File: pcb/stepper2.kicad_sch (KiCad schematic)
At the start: 61 parts, among them J1 DA15_Receptacle_MountingHoles, J10 Conn_01x07_Pin, J11 FAN, J12 Conn_01x03_Pin, J13 Conn_01x03_Pin, J14 Conn_01x03_Pin, J2 DA15_Receptacle_MountingHoles, J3 DA15_Receptacle_MountingHoles, J4 DE15_Receptacle_HighDensity, J5 DE15_Receptacle_HighDensity, J6 DE15_Receptacle_HighDensity, J7 Conn_01x04_Pin, J8 Conn_01x05_Pin, J9 Conn_01x06_Pin, SW1 SW_Push, U1 AM26LS32ACN, U2 AM26LS32Ax, U3 AM26LS32ACN, U4 TMC2209_BIGTREETECH, U5 TMC2209_BIGTREETECH, U6 TMC2209_BIGTREETECH

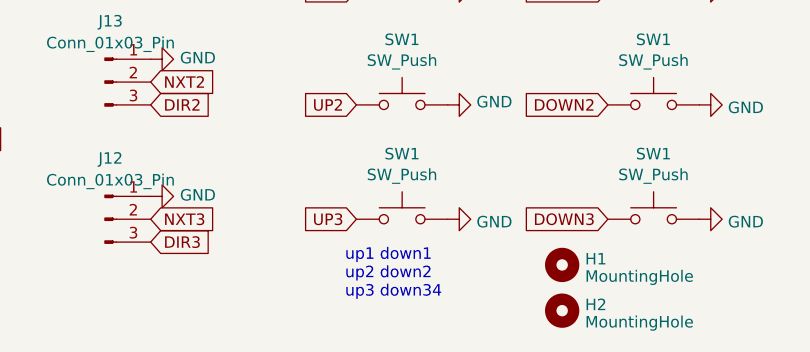
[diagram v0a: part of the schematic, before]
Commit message: fixed typo in schematics
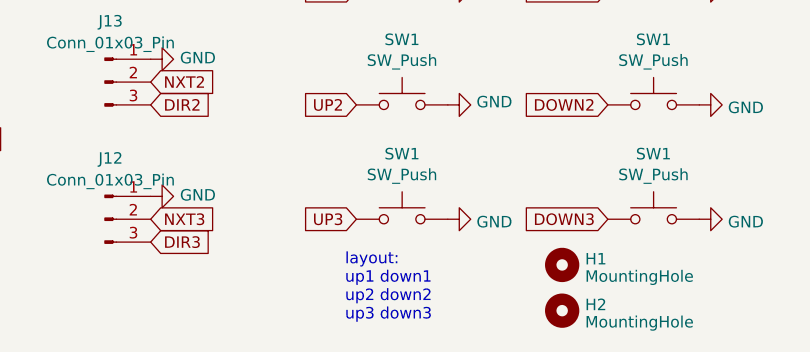
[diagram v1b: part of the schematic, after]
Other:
- note added: "layout: up1 down1 up2 down2 up3 down3"
- note removed: "up1 down1 up2 down2 up3 down34"
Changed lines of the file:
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@@
     (stroke (width 0) (type default))
   )
-  (text "up1 down1\nup2 down2\nup3 down34\n" (at 125.73 194.31 0)
+  (text "layout:\nup1 down1\nup2 down2\nup3 down3\n" (at 125.73 196.85 0)
     (effects (font (size 1.27 1.27)) (justify left bottom))
   )

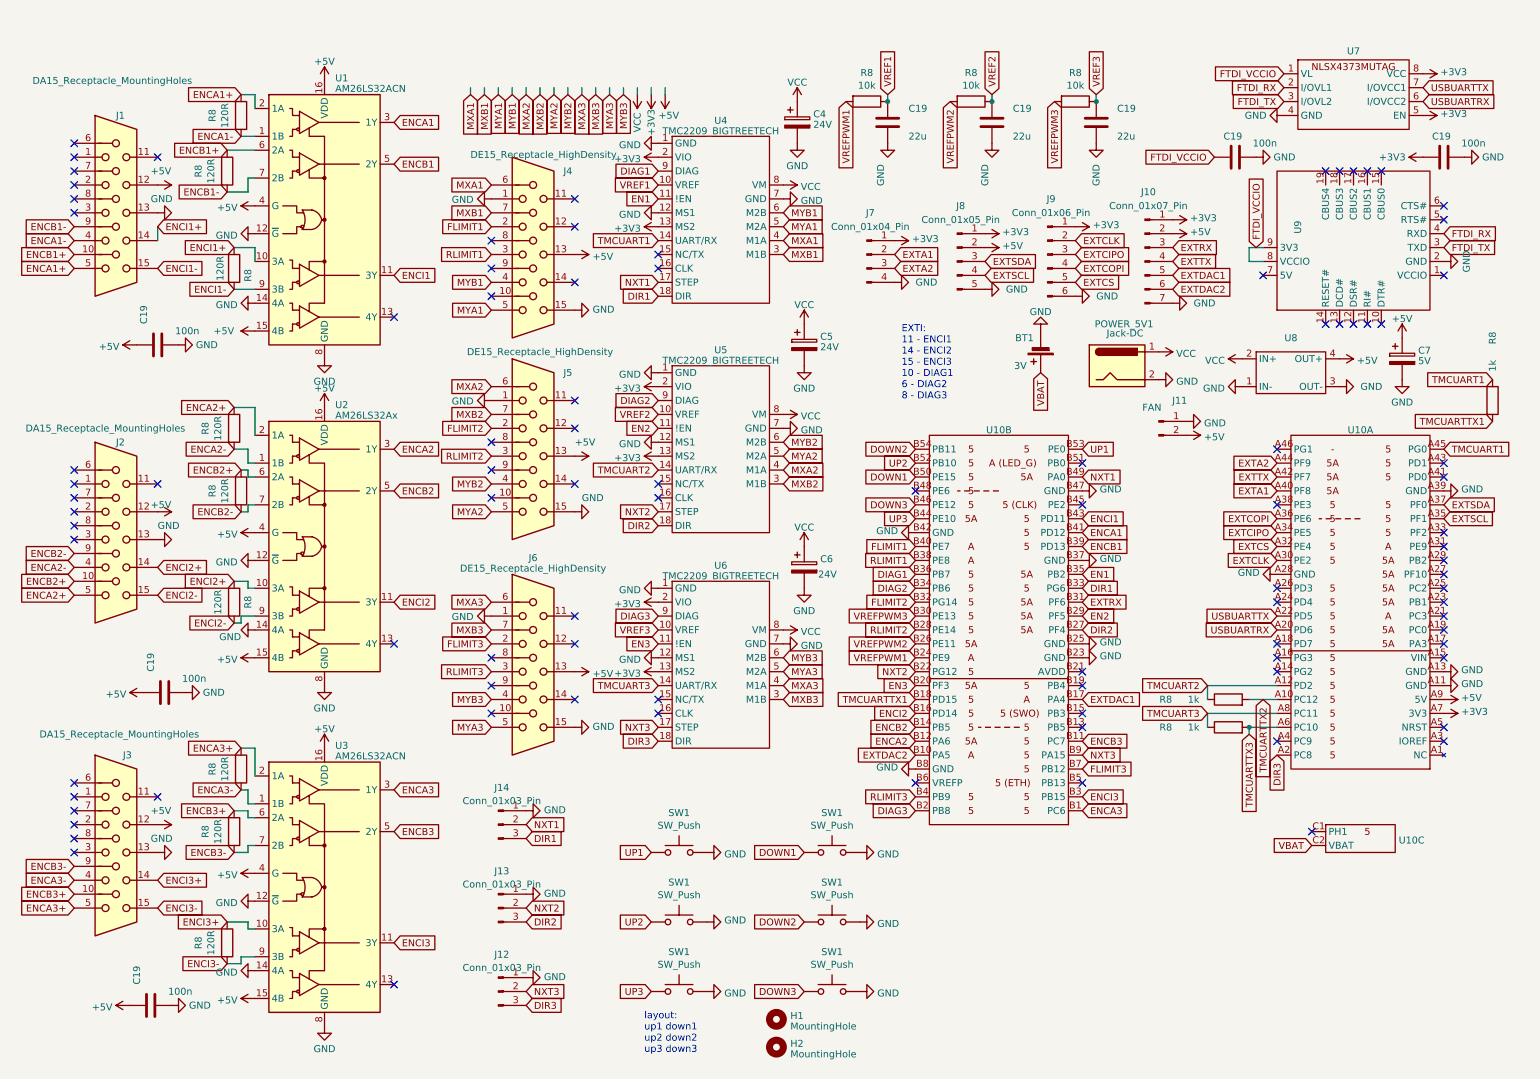
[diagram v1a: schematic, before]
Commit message: PCB updated to use active and available components; added mpn numbers
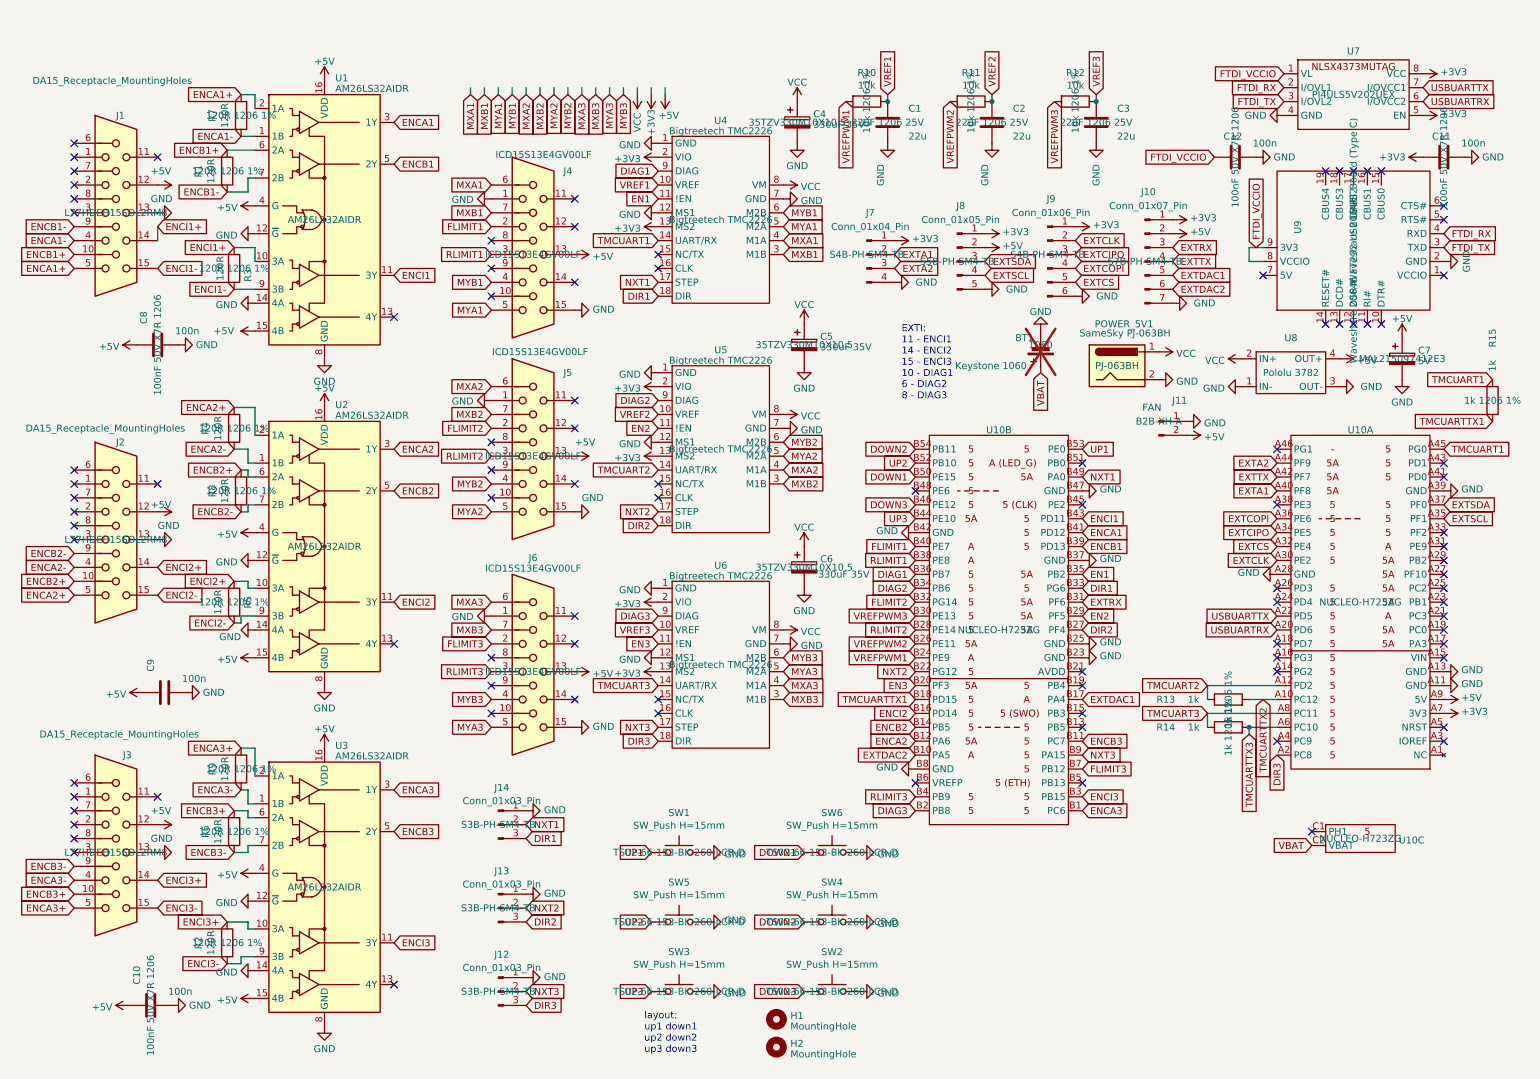
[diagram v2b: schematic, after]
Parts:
- BT1: value 3V -> Keystone 1060; mpn (none) -> 1060; now not fitted
- C1, C2, C3: renamed from C19; mpn (none) -> 22uF 1206 25V
- C10, C11, C12, C8, C9: renamed from C19; mpn (none) -> 100nF 50V X7R 1206
- C4, C5, C6: value 24V -> 330uF 35V; mpn (none) -> 35TZV330M10X10.5
- C7: mpn (none) -> MAL215097412E3
- J1, J2, J3: mpn (none) -> L77HDEH15SOL2RM8
- J10: mpn (none) -> S7B-PH-SM4-TB
- J11: mpn (none) -> B2B-XH-A
- J12, J13, J14: mpn (none) -> S3B-PH-SM4-TB
- J4, J5, J6: value DE15_Receptacle_HighDensity -> ICD15S13E4GV00LF; mpn (none) -> ICD15S13E4GV00LF
- J7, J9: mpn (none) -> S4B-PH-SM4-TB
- J8: mpn (none) -> S5B-PH-SM4-TB
- POWER_5V1: value Jack-DC -> SameSky PJ-063BH; mpn (none) -> PJ-063BH
- R1, R2, R3, R4, R5, R6, R7, R9: renamed from R8; mpn (none) -> 120R 1206 1%
- R10, R11, R12: renamed from R8; mpn (none) -> 10k 1206 1%
- R13, R14, R15: renamed from R8; mpn (none) -> 1k 1206 1%
- R8: mpn (none) -> 120R 1206 1%
- SW1: value SW_Push -> SW_Push H=15mm; footprint Button_Switch_SMD:SW_Push_1P1T_NO_6x6mm_H9.5mm -> Button_Switch_THT:SW_PUSH_6mm_H4.3mm; LCSC C620327 -> (none); mpn (none) -> TS02-66-153-BK-260-LCR-D
- SW2, SW3, SW4, SW5, SW6: renamed from SW1; value SW_Push -> SW_Push H=15mm; footprint Button_Switch_SMD:SW_Push_1P1T_NO_6x6mm_H9.5mm -> Button_Switch_THT:SW_PUSH_6mm_H4.3mm; LCSC C620327 -> (none); mpn (none) -> TS02-66-153-BK-260-LCR-D
- U1, U3: value AM26LS32ACN -> AM26LS32AIDR; mpn (none) -> AM26LS32AIDR
- U10: mpn (none) -> NUCLEO-H723ZG
- U2: value AM26LS32Ax -> AM26LS32AIDR; mpn (none) -> AM26LS32AIDR
- U4, U5, U6: value TMC2209_BIGTREETECH -> Bigtreetech TMC2226; mpn (none) -> Bigtreetech TMC2226
- U7: footprint stepper2:UDFN-8_1.2x1.8mm_OR_SO8_3.9x4.9mm -> Package_SO:MSOP-8_3x3mm_P0.65mm; LCSC C604194 -> C481697; mpn (none) -> PI4ULS5V202UEX
- U8: footprint stepper2:DCDC_17.0mm_22.2mm -> stepper2:POLOLU_3782; mpn (none) -> Pololu 3782
- U9: value ~ -> Waveshare 20646 FT232 USB UART Board (Type C); mpn (none) -> Waveshare 20646

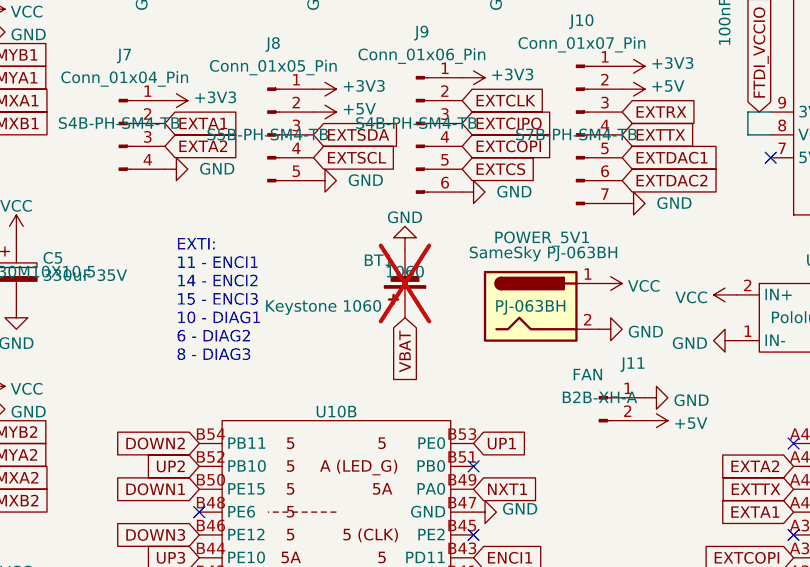
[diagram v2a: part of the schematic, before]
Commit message: reverted DNP flag for 3V battery
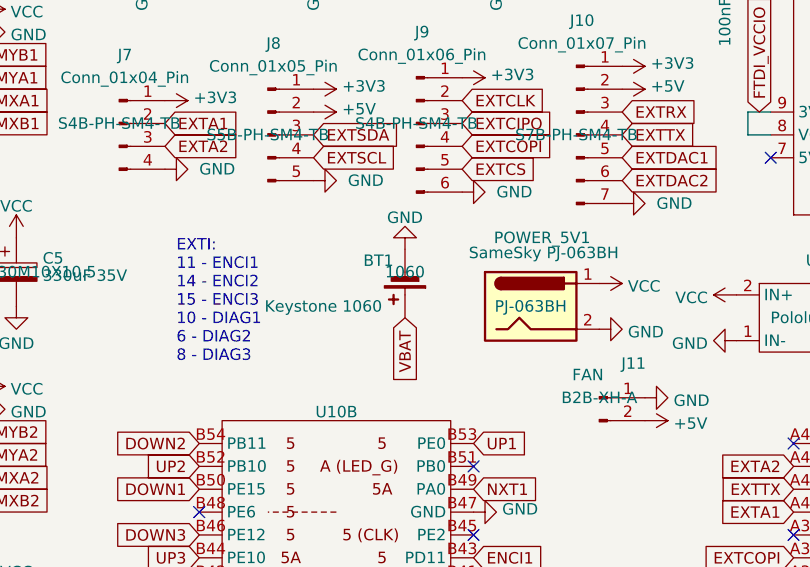
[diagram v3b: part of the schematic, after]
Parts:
- BT1: now fitted
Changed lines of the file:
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@@
 		(in_bom yes)
 		(on_board yes)
-		(dnp yes)
+		(dnp no)
 		(property "Reference" "BT1"
 			(at 196.85 66.04 0)

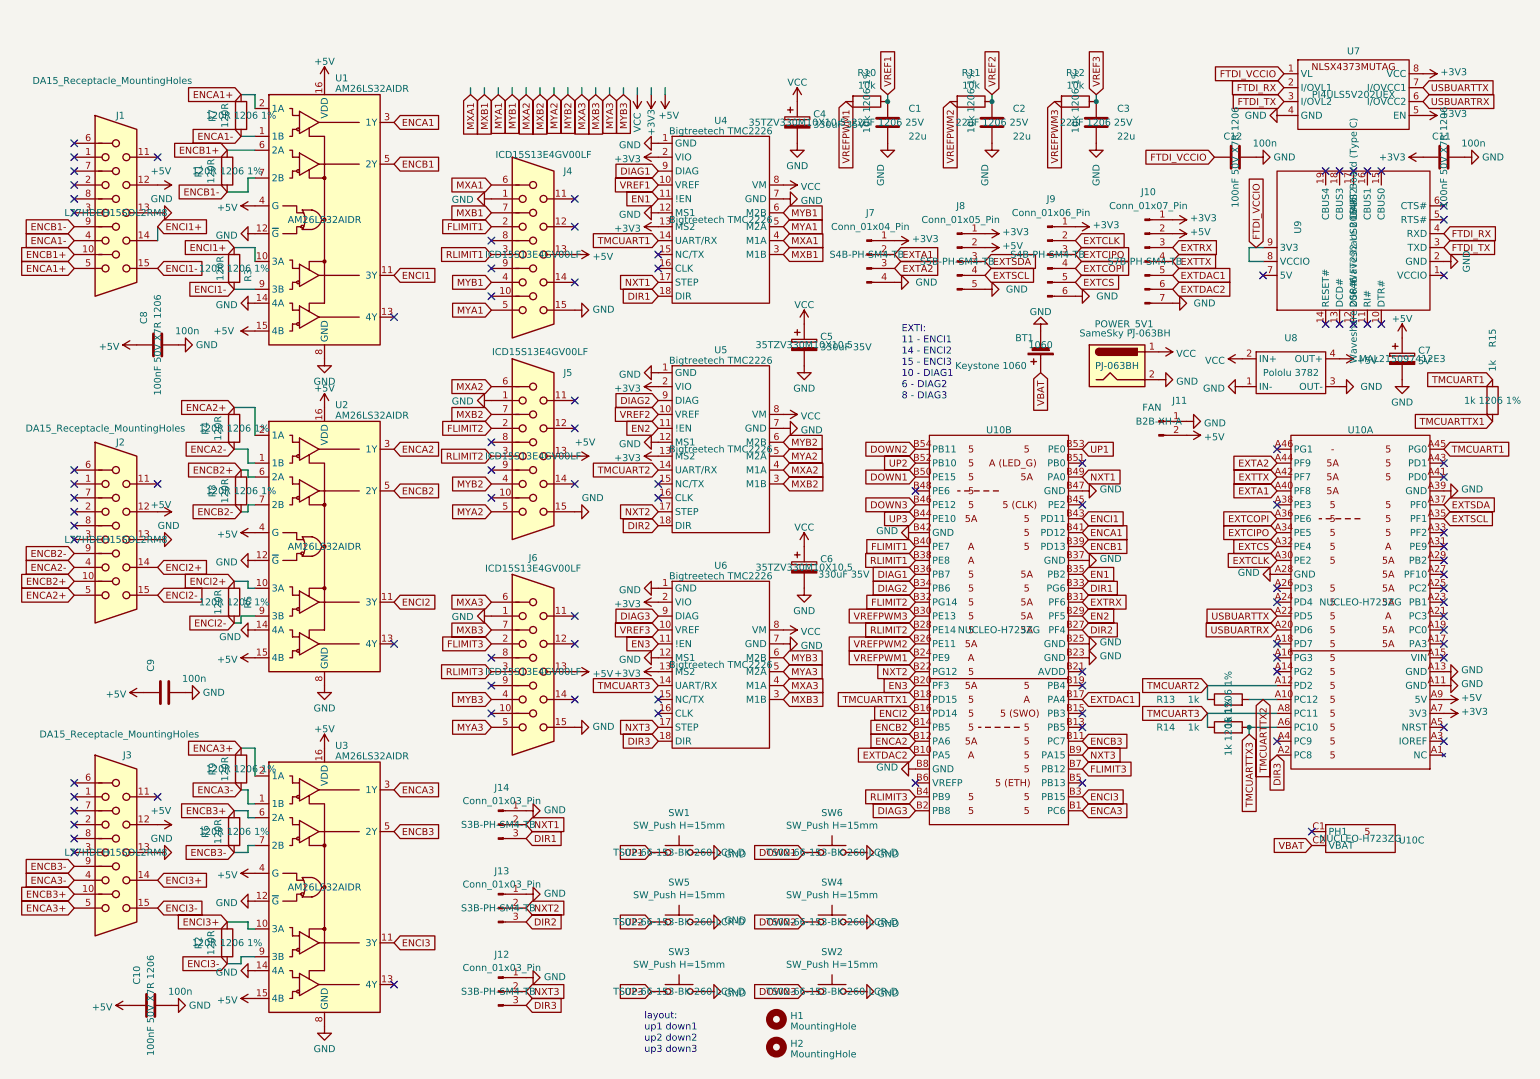
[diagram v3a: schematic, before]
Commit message: non-standard components marked as DNP for easier assembly ordering
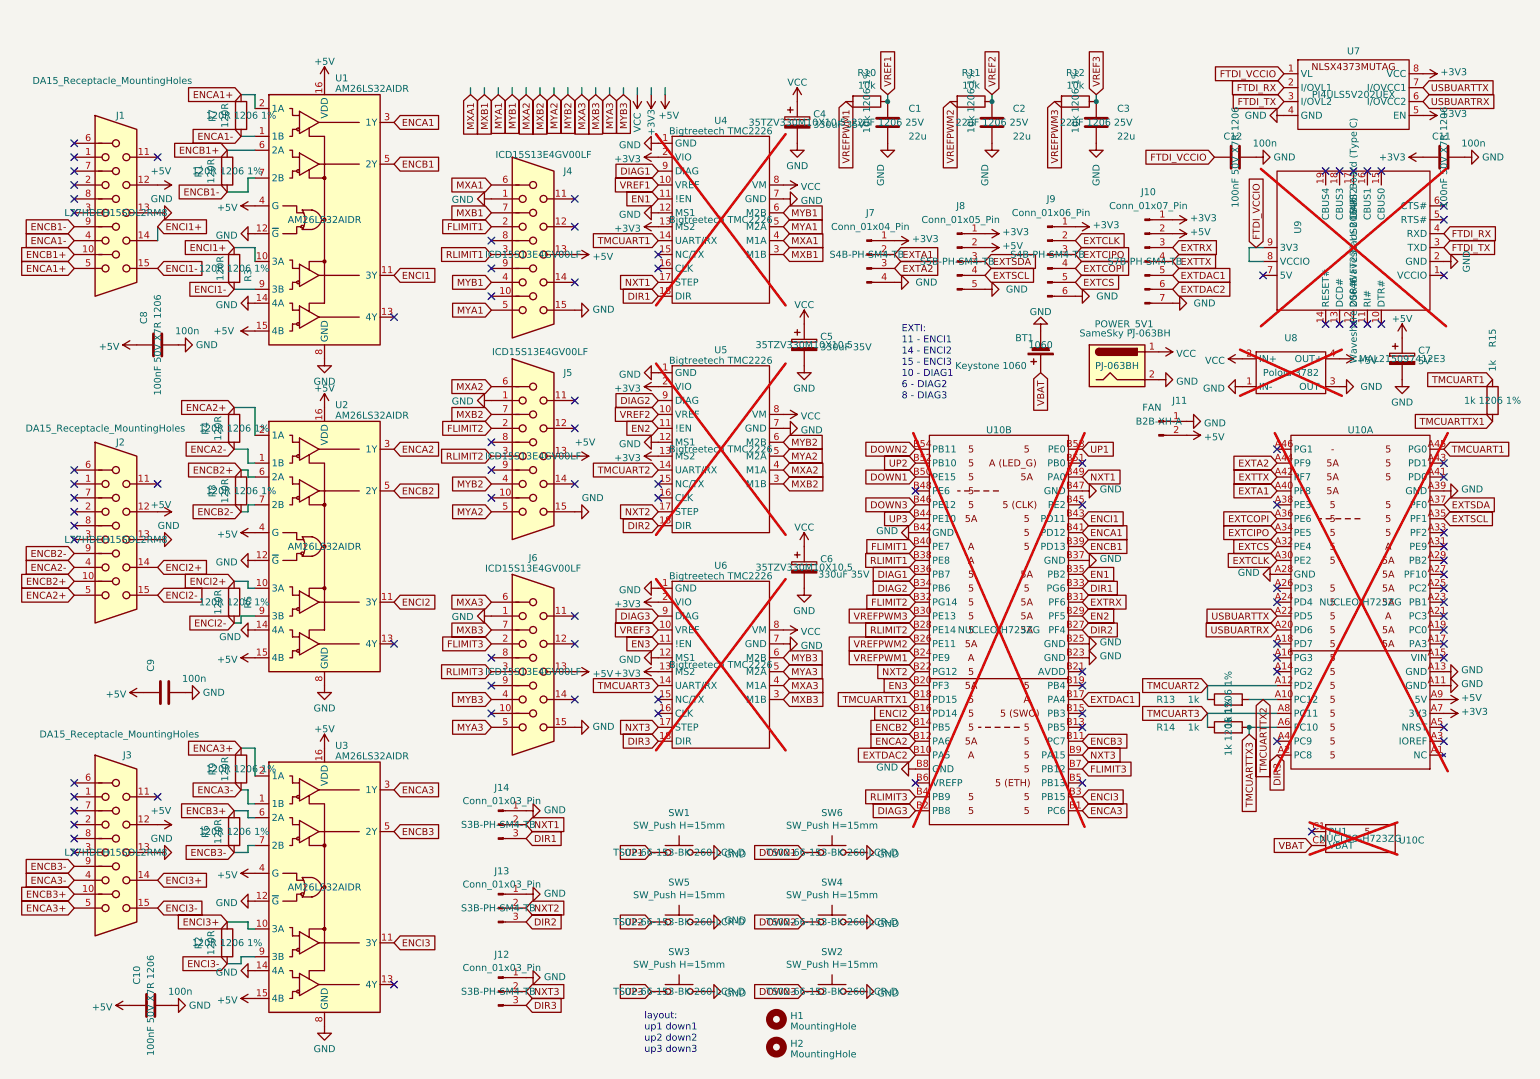
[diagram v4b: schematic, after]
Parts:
- U10, U4, U5, U6, U8, U9: now not fitted
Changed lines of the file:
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@@
 		(in_bom yes)
 		(on_board yes)
-		(dnp no)
+		(dnp yes)
 		(fields_autoplaced yes)
 		(property "Reference" "U10"
@@
 		(in_bom yes)
 		(on_board yes)
-		(dnp no)
+		(dnp yes)
 		(fields_autoplaced yes)
 		(property "Reference" "U10"
@@
 		(in_bom yes)
 		(on_board yes)
-		(dnp no)
+		(dnp yes)
 		(fields_autoplaced yes)
 		(property "Reference" "U5"
@@
 		(in_bom yes)
 		(on_board yes)
-		(dnp no)
+		(dnp yes)
 		(fields_autoplaced yes)
 		(property "Reference" "U4"
@@
 		(in_bom no)
 		(on_board yes)
-		(dnp no)
+		(dnp yes)
 		(fields_autoplaced yes)
 		(property "Reference" "U8"
@@
 		(in_bom no)
 		(on_board yes)
-		(dnp no)
+		(dnp yes)
 		(property "Reference" "U9"
 			(at 245.11 46.99 0)
@@
 		(in_bom yes)
 		(on_board yes)
-		(dnp no)
+		(dnp yes)
 		(fields_autoplaced yes)
 		(property "Reference" "U10"
@@
 		(in_bom yes)
 		(on_board yes)
-		(dnp no)
+		(dnp yes)
 		(fields_autoplaced yes)
 		(property "Reference" "U6"

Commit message: updated symbol for level shifter
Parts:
- U7: symbol stepper2:NLSX4373MUTAG -> stepper2:PI4ULS5V202UEX
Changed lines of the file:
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@@
 	)
 	(symbol
-		(lib_id "stepper2:NLSX4373MUTAG")
+		(lib_id "stepper2:PI4ULS5V202UEX")
 		(at 255.27 21.59 0)
 		(unit 1)
@@
 		(fields_autoplaced yes)
 		(property "Reference" "U7"
-			(at 255.27 13.6469 0)
+			(at 255.27 7.62 0)
 			(effects
 				(font
@@
 		)
 		(property "Value" "~"
-			(at 255.27 21.59 0)
+			(at 255.27 10.16 0)
 			(effects
 				(font
@@
 					(size 1.27 1.27)
 				)
+				(hide yes)
 			)
 		)
@@
 		)
 		(property "mpn" "PI4ULS5V202UEX"
-			(at 255.27 21.59 0)
+			(at 255.27 12.7 0)
 			(effects
 				(font
